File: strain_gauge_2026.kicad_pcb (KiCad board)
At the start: 2 copper layers, 62.5 x 41.5 mm, 29 parts, among them J2 Conn_01x04_Socket, J3 Conn_01x04_Socket, J5 Conn_01x04_Socket, U1 NAU7802SGI

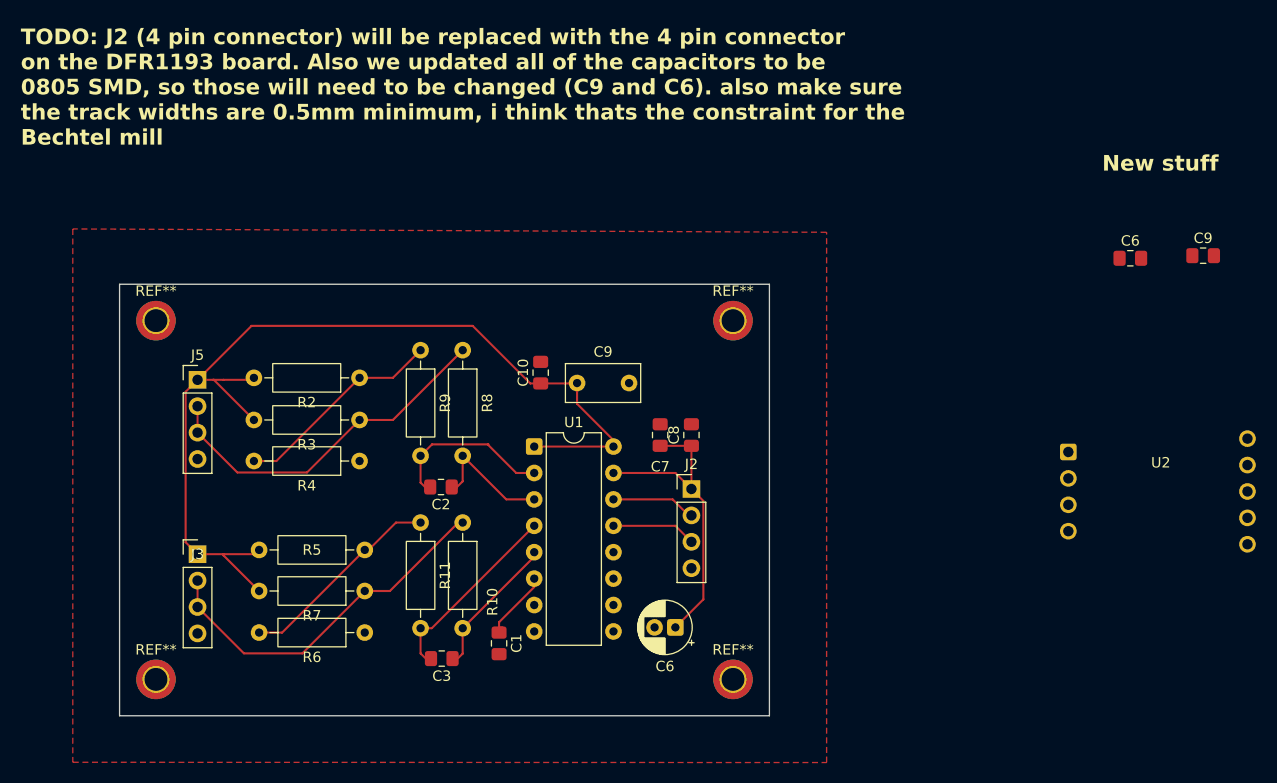
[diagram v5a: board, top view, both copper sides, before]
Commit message: Integrated I2C translator board into PCB Layout and adjusted placement of components
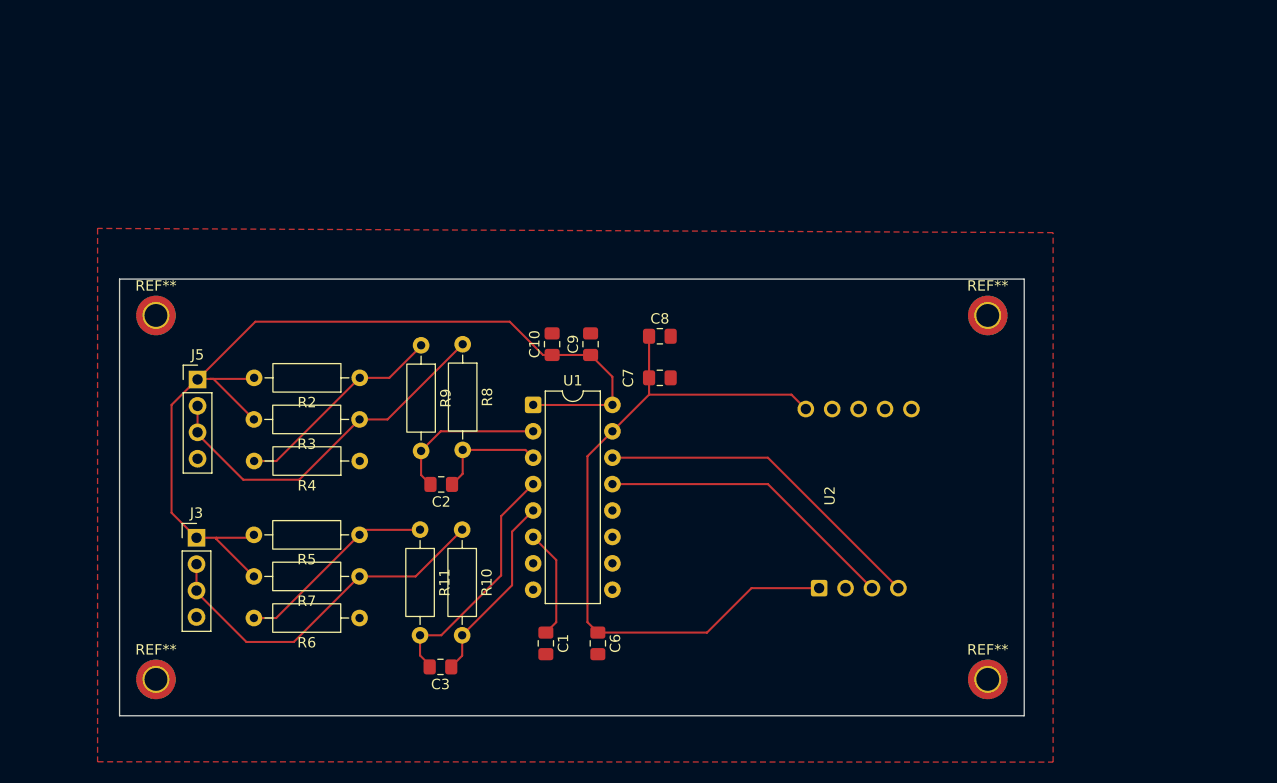
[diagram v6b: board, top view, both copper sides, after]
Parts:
- removed the C6 at (167.5, 111.0)
- removed the C9 at (158.0, 87.5)
- removed J2: Conn_01x04_Socket, Connector_PinHeader_2.54mm:PinHeader_1x04_P2.54mm_Vertical
- moved C6 63.2 mm to (160.0, 112.5), turned to -90 degrees
- moved C9 59.5 mm to (159.3, 83.8), turned to 90 degrees
- moved U2 27.3 mm to (181.3, 107.2), turned to 90 degrees
- moved REF** 24.5 mm to (197.5, 81.0)
- moved REF** 24.5 mm to (197.5, 116.0)
- moved C8 9.97 mm to (166.0, 83.0), turned to 0 degrees
- moved C7 5.50 mm to (166.0, 87.0), turned to 0 degrees
- moved C1 4.50 mm to (155.0, 112.5)
- moved U1 4.01 mm to (153.8, 89.6)
- moved C10 2.95 mm to (155.6, 83.8)
- moved J3 1.58 mm to (121.4, 102.4)
- moved R5 1.53 mm to (137.1, 102.1)
- moved R6 1.49 mm to (137.1, 110.1)
- moved R7 1.49 mm to (137.1, 106.1)
- moved C3 0.81 mm to (144.9, 114.8)
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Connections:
- U1 pad 13: SCLK_MCU -> SCLK
- U1 pad 14: SDA_MCU -> SDA
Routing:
- net +3V3: track 30.6 -> 70.1 mm
- net SDA: track 0.00 -> 32.7 mm
- net SCLK: track 0.00 -> 29.1 mm
- net SDA_MCU: track 8.29 -> 0.00 mm
- net SCLK_MCU: track 8.29 -> 0.00 mm
- net Net-(U1-VIN2N): track 18.8 -> 23.6 mm
- net Net-(U1-VBG): track 6.43 -> 10.9 mm
- net Net-(U1-VIN2P): track 14.0 -> 18.2 mm
- net V_excitation: track 96.8 -> 94.0 mm
- net Net-(U1-VIN1P): track 12.6 -> 10.8 mm
- net Net-(U1-VIN1N): track 16.5 -> 15.2 mm
- net A+: track 34.5 -> 35.5 mm
- net B-: track 20.4 -> 19.5 mm
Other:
- board size 62.5 x 41.5 mm -> 87 x 42 mm
- board text removed: "New stuff"
- board text removed: "TODO: J2 (4 pin connector) will be replaced with the 4 pin connector on the DFR1193 board. Also we updated all of the capacitors to be 0805 SMD, so those will need to be changed (C9 and C6). also make sure the track widths are 0.5mm minimum, i think thats the constraint for the Bechtel mill"

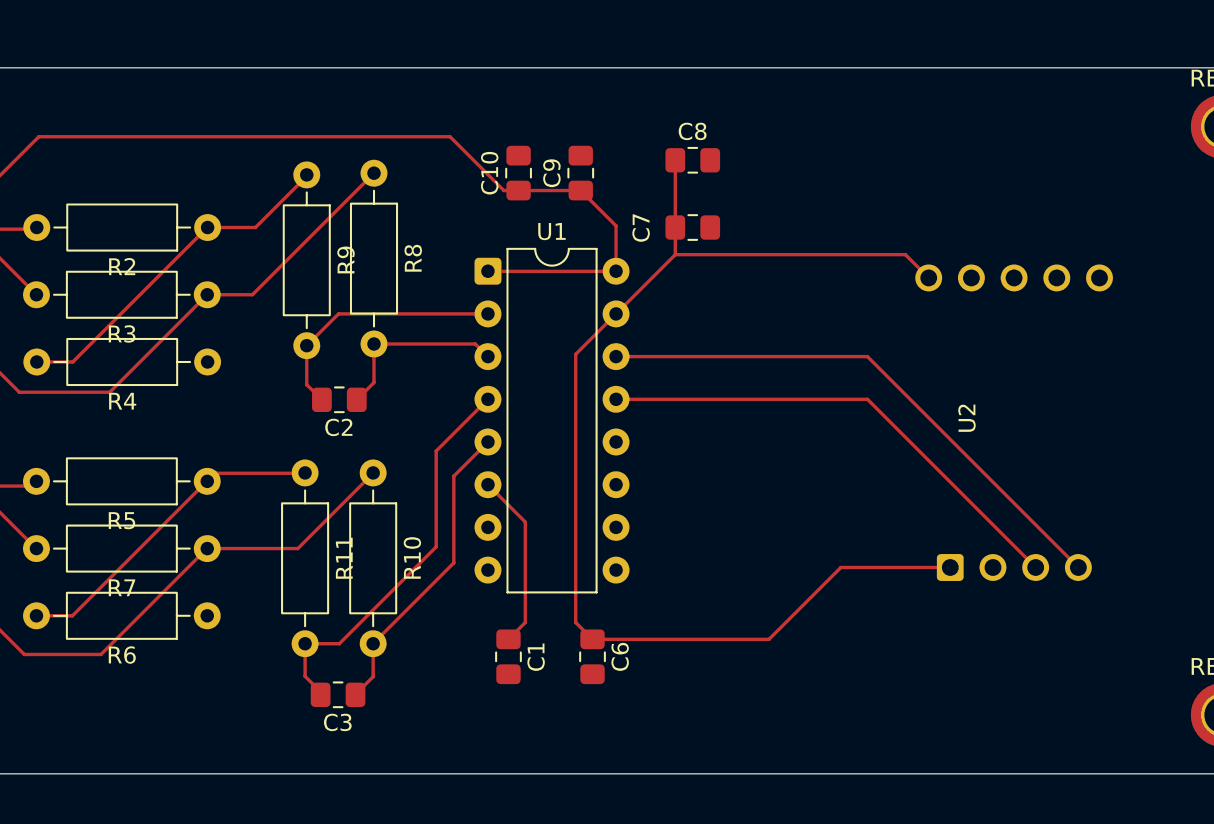
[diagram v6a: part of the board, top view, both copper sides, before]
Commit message: Resolved DRC errors
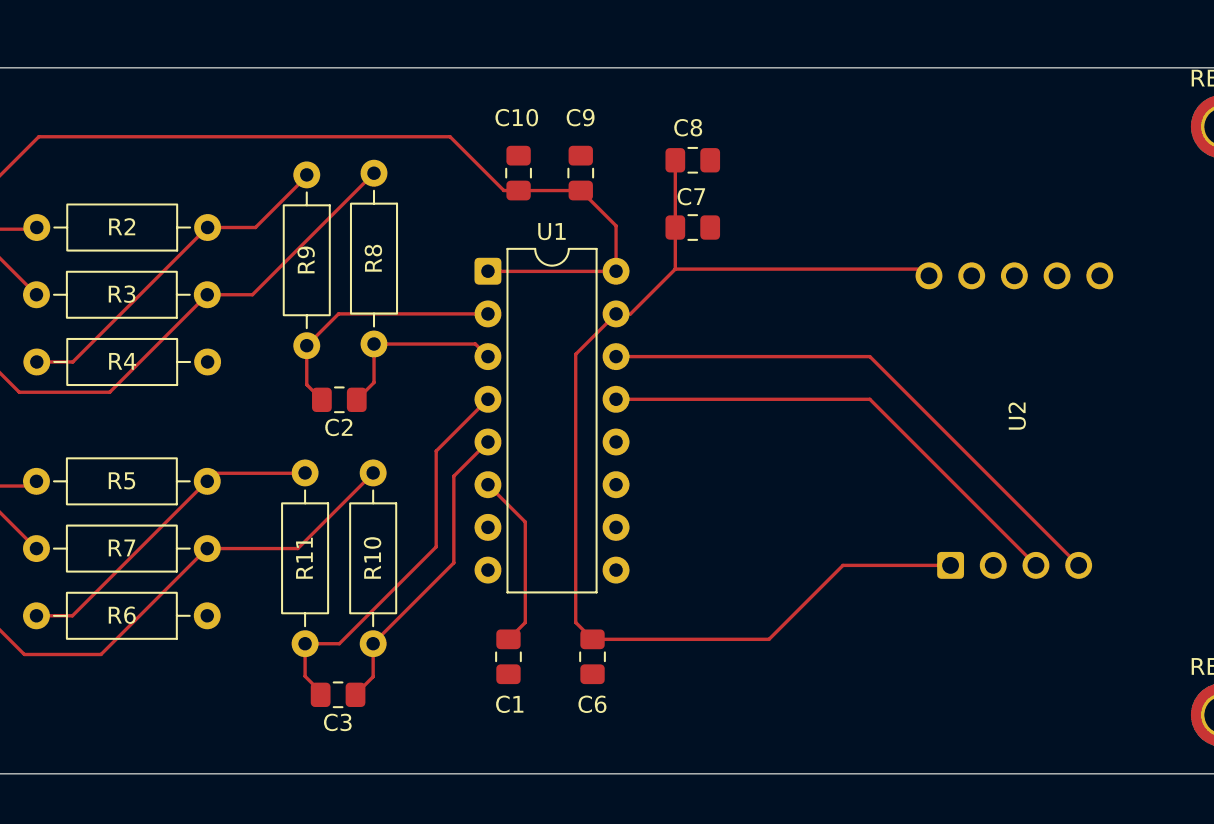
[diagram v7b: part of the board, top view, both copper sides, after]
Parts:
- moved U2 0.13 mm to (181.3, 107.1)

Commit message: Moved traces, fills, and SMD to B.Cu, and increased trace width
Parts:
- C1, C10, C2, C3, C6, C7, C8, C9: moved to B.Cu
- moved C8 7.16 mm to (170.5, 88.5), turned to 90 degrees
- moved U2 4.02 mm to (177.3, 107.0)
- moved REF** 4.00 mm to (193.5, 116.0)
- moved REF** 4.00 mm to (193.5, 81.0)
- moved C7 1.63 mm to (166.5, 88.5), turned to 90 degrees
- moved REF** 1.00 mm to (118.5, 116.0)
- moved REF** 1.00 mm to (118.5, 81.0)
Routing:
- net +3V3: track 70.3 -> 55.9 mm
- net SDA: track 32.7 -> 28.6 mm
- net SCLK: track 29.1 -> 25.0 mm
- net Net-(U1-VIN1N): track 15.2 -> 15.8 mm
- added copper zone on B.Cu, net GND
- removed copper zone on F.Cu, net GND
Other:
- board size 87 x 42 mm -> 82 x 42 mm
- board text added: "TODO: label dimensions on User.Drawings layer make traces thicker (minimum 0.5mm, 0.75-1 reccommended) Move copper and SMD components to Back Copper, leave THT components on the front"
